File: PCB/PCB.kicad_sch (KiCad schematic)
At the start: 21 parts, among them J1 Conn_01x06_Female, U13 74HC165, U15 LT3042xMSE, U16 74HC165

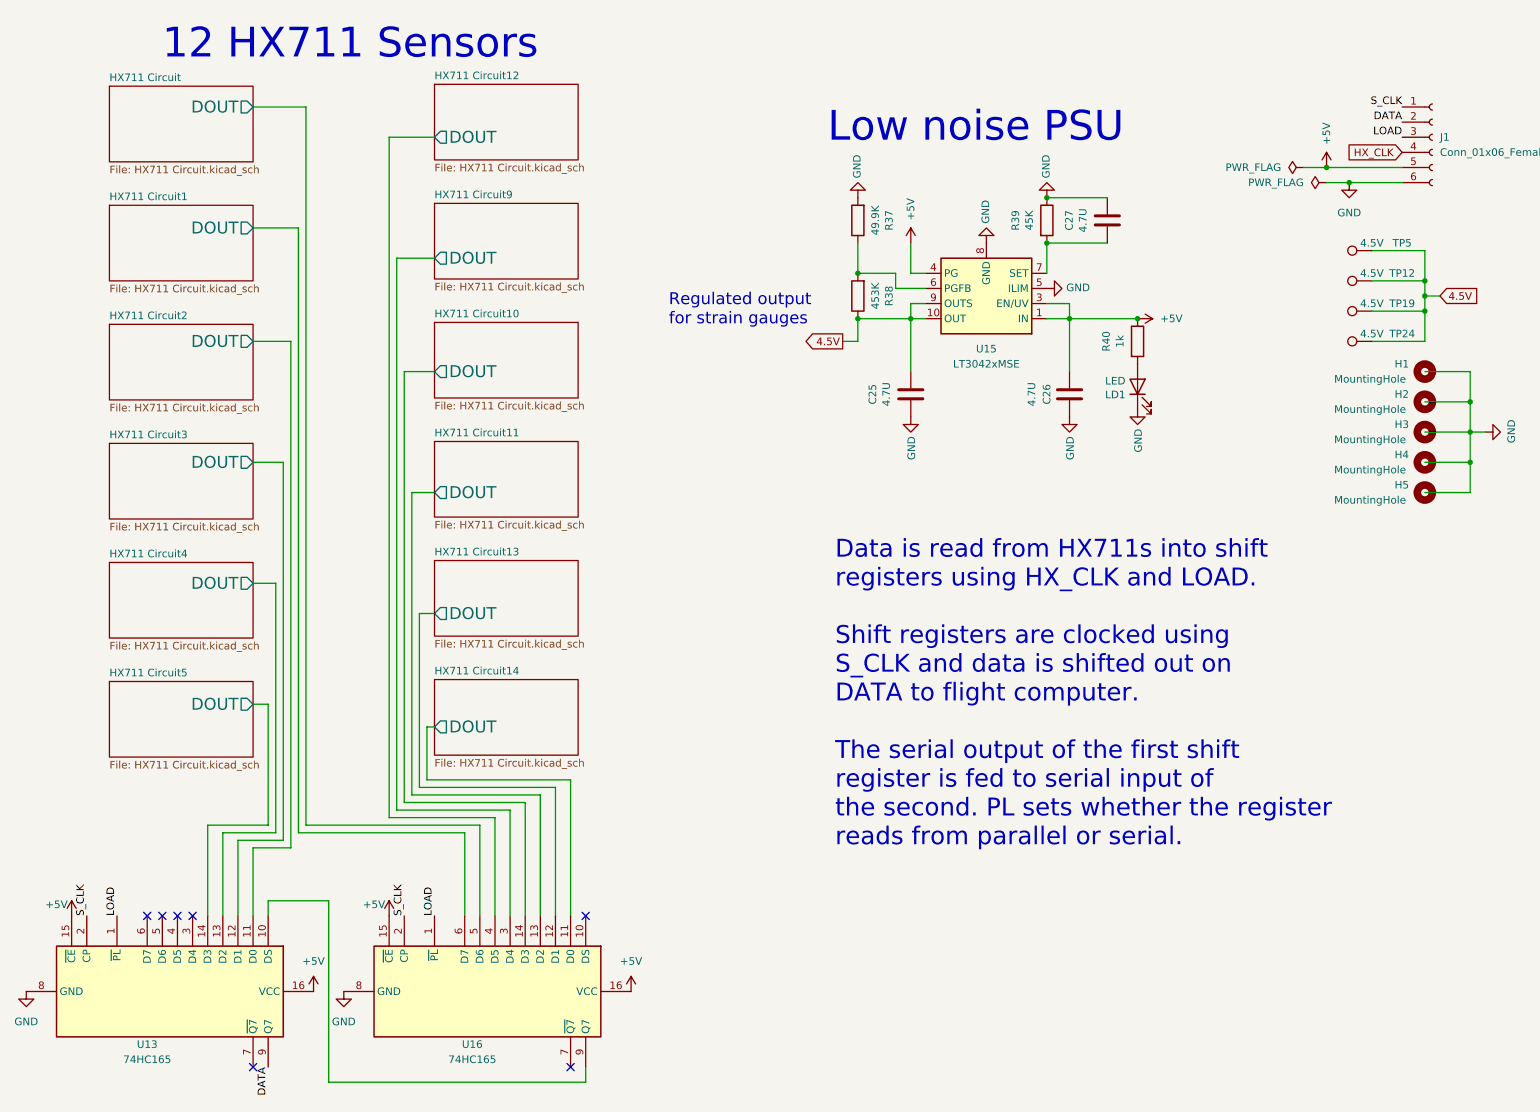
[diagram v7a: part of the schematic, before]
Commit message: Fix _CE so it is now LOW
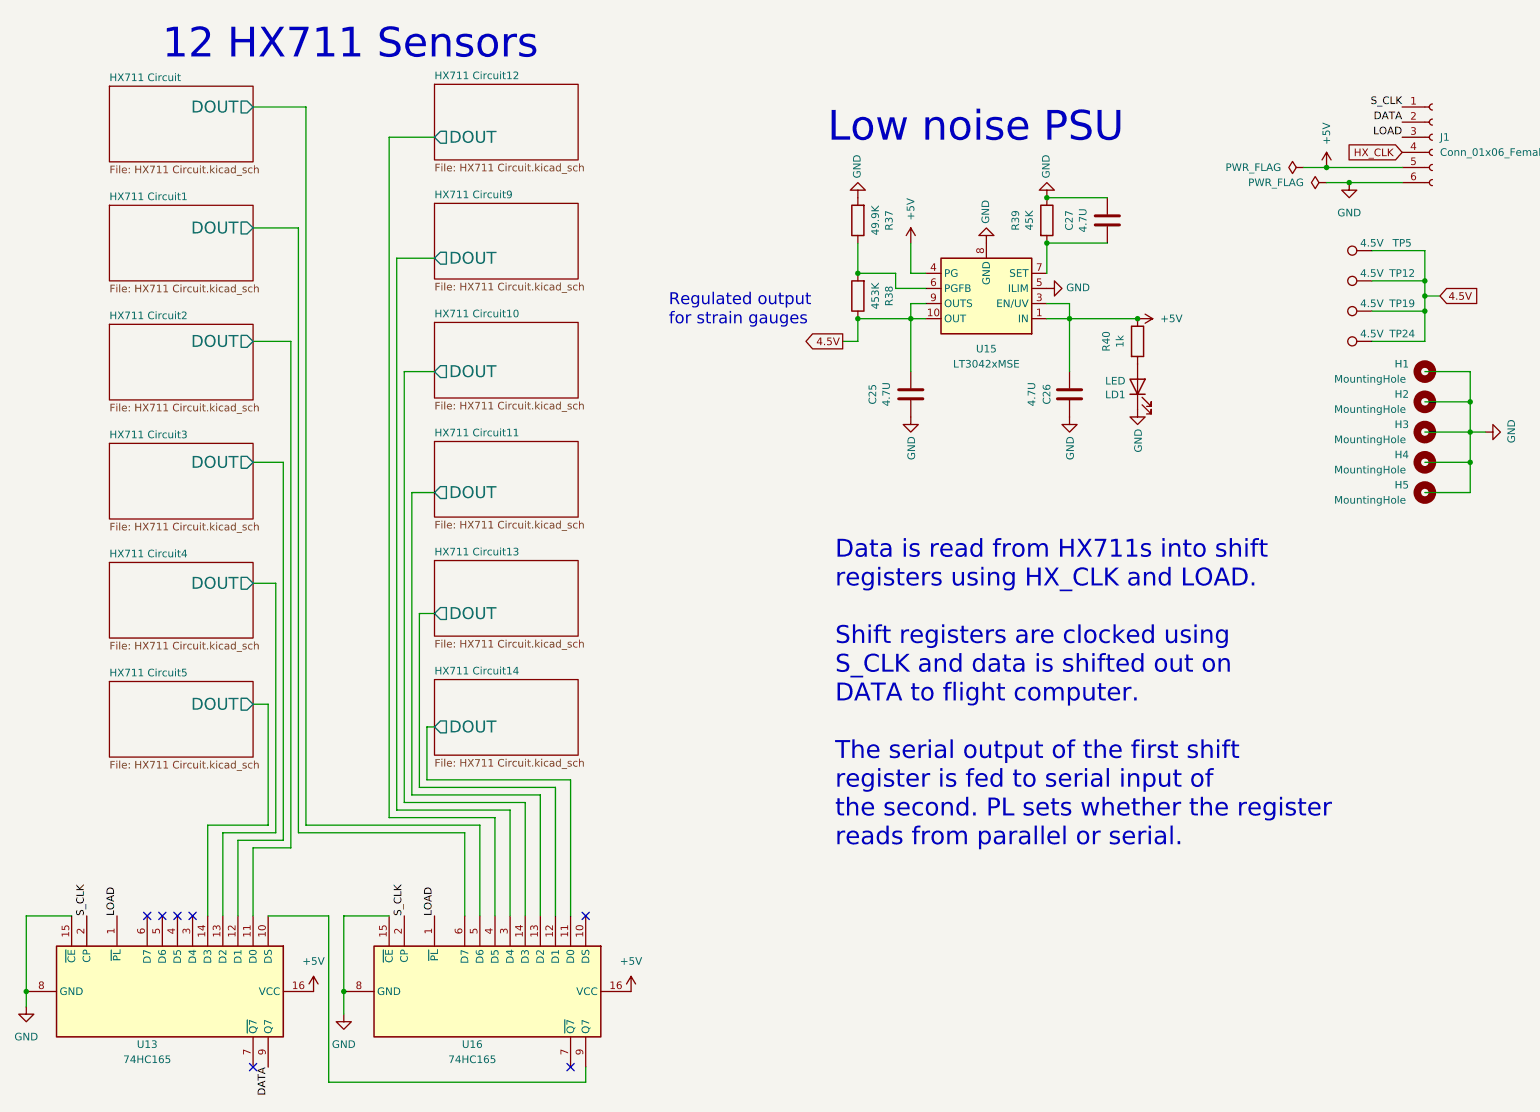
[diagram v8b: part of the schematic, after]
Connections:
- net +5V: no longer U13.15 (~{CE}), U16.15 (~{CE})
- net GND: now also U13.15 (~{CE}), U16.15 (~{CE})
